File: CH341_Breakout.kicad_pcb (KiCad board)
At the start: 2 copper layers, 4 parts, among them J01 CONN_MODE, J11 CONN_I2C, J12 CONN_UART, J13 CONN_SPI

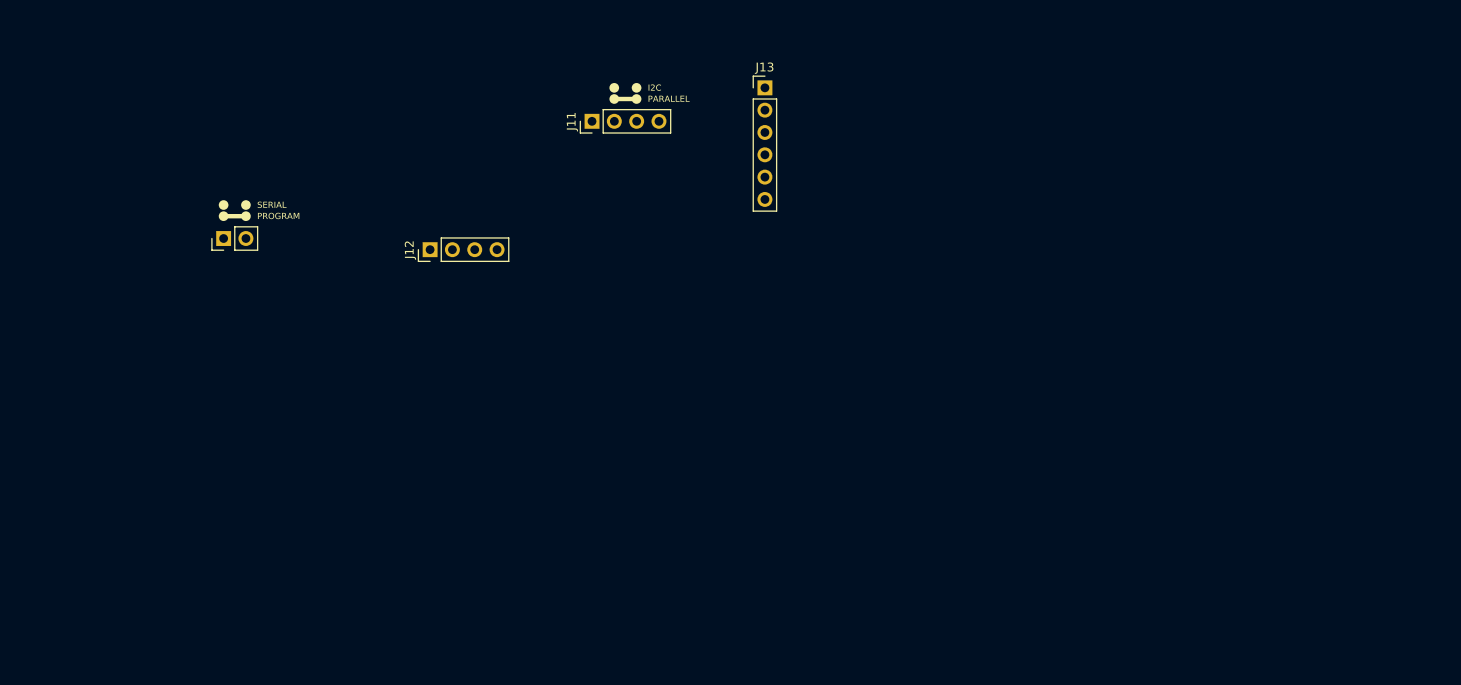
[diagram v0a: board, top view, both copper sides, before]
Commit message: Added USB C and other bits
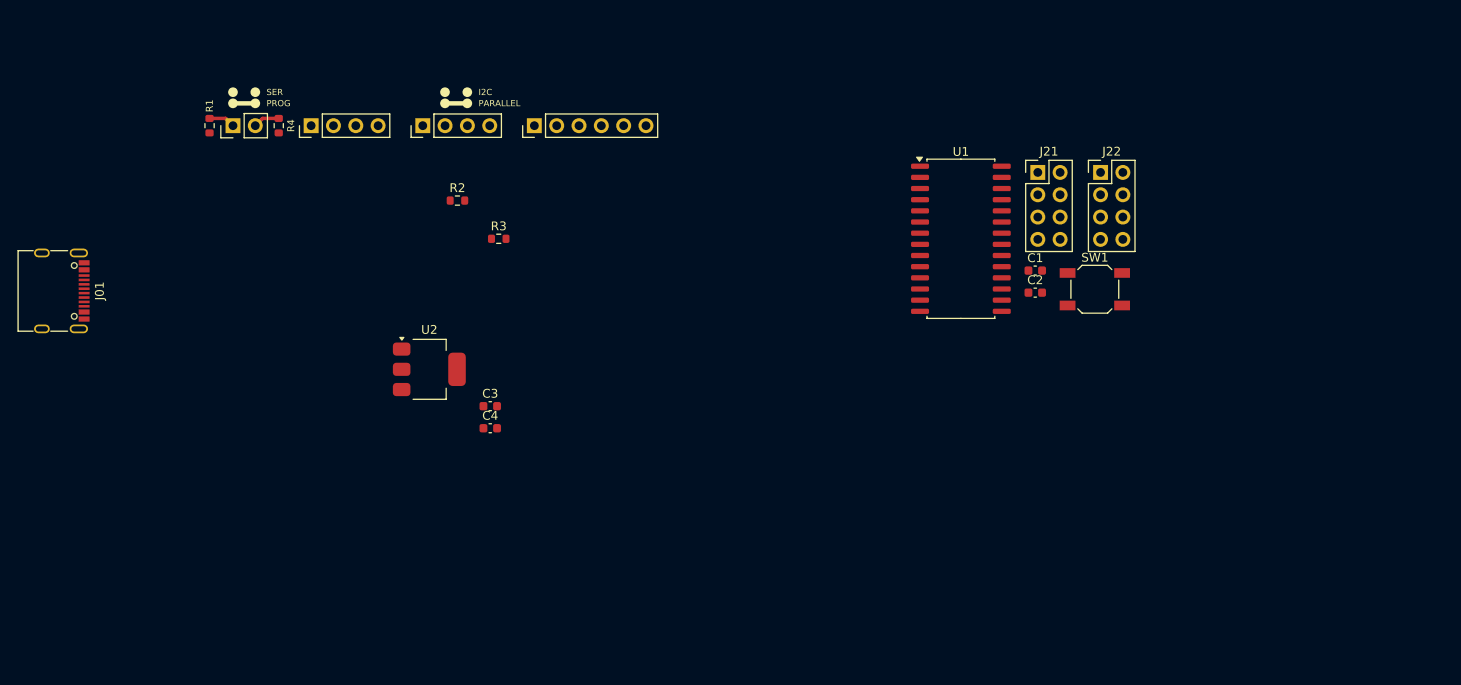
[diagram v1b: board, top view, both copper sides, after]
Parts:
- added C1: 20pF, Capacitor_SMD:C_0603_1608Metric, F.Cu at (131.1, 44.3)
- added C2: 20pF, Capacitor_SMD:C_0603_1608Metric, F.Cu at (131.1, 46.8)
- added C3: 100nF, Capacitor_SMD:C_0603_1608Metric, F.Cu at (69.1, 59.7)
- added C4: 100nF, Capacitor_SMD:C_0603_1608Metric, F.Cu at (69.1, 62.2)
- added J02: CONN_MODE, Connector_PinHeader_2.54mm:PinHeader_1x02_P2.54mm_Vertical, F.Cu at (39.8, 27.8)
- added J21: CONN_SPI_FLASH, Connector_PinHeader_2.54mm:PinHeader_2x04_P2.54mm_Vertical, F.Cu at (131.4, 33.1)
- added J22: CONN_I2C_EEPROM, Connector_PinHeader_2.54mm:PinHeader_2x04_P2.54mm_Vertical, F.Cu at (138.5, 33.1)
- added R1: 2K2, Resistor_SMD:R_0603_1608Metric, F.Cu at (37.1, 27.8)
- added R2: 2K2, Resistor_SMD:R_0603_1608Metric, F.Cu at (65.3, 36.3)
- added R3: 2K2, Resistor_SMD:R_0603_1608Metric, F.Cu at (70.0, 40.7)
- added R4: 2K2, Resistor_SMD:R_0603_1608Metric, F.Cu at (45.0, 27.8)
- added SW1: SW_SPST, Button_Switch_SMD:SW_SPST_SKQG_WithoutStem, F.Cu at (137.9, 46.4)
- added U1: CH341A, Package_SO:SOIC-28W_7.5x17.9mm_P1.27mm, F.Cu at (122.6, 40.7)
- added U2: AMS1117-3.3, Package_TO_SOT_SMD:SOT-223-3_TabPin2, F.Cu at (62.1, 55.5)
- J01: value CONN_MODE -> USB_C; footprint Connector_PinHeader_2.54mm:PinHeader_1x02_P2.54mm_Vertical -> Connector_USB:USB_C_Receptacle_G-Switch_GT-USB-7010ASV
- moved J13 26.6 mm to (74.1, 27.8), turned to 90 degrees
- moved J01 20.5 mm to (19.1, 46.6), turned to -90 degrees
- moved J12 19.6 mm to (48.7, 27.8)
- moved J11 19.3 mm to (61.4, 27.8)
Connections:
- J11 pad 4: /A0 -> GND
- J12 pad 4: /A0 -> GND
- J13 pad 6: /A0 -> GND
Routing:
- net Net-(J02-Pin_2): track 0.00 -> 3.01 mm
- net /ACT#: track 0.00 -> 3.01 mm
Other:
- board text added: "3V3"
- board text added: "CS"
- board text added: "GND"
- board text added: "MISO"
- board text added: "MOSI"
- board text added: "PROG"
- board text added: "RX"
- board text added: "SCL"
- board text added: "SCLK"
- board text added: "SDA"
- board text added: "SER"
- board text added: "TX"
- board text removed: "PROGRAM"
- board text removed: "SERIAL"

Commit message: Started MkI PCB Design
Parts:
- removed C4: 100nF, Capacitor_SMD:C_0603_1608Metric
- removed the J11 at (61.4, 27.8)
- removed the J13 at (74.1, 27.8)
- added D1: ACT, LED_SMD:LED_0603_1608Metric, F.Cu at (174.3, 84.3)
- added D2: PWR, LED_SMD:LED_0603_1608Metric, F.Cu at (174.3, 87.5)
- added Y1: 12MHz, Crystal:Crystal_HC49-U_Vertical, F.Cu at (153.9, 75.5)
- J12: renamed from J22; value CONN_I2C_EEPROM -> CONN_SPI_FLASH
- SW1: value SW_SPST -> RST
- moved J01 148.8 mm to (163.0, 84.7), turned to 0 degrees
- moved R1 147.8 mm to (174.3, 82.7), turned to 180 degrees
- moved J02 144.3 mm to (174.3, 80.1), turned to 180 degrees
- moved R4 137.6 mm to (174.3, 74.9), turned to 0 degrees
- moved J11 132.1 mm to (174.3, 68.7), turned to 180 degrees
- moved R2 119.7 mm to (174.3, 85.9), turned to 180 degrees
- moved C3 98.4 mm to (167.5, 59.8), turned to 180 degrees
- moved U2 95.3 mm to (153.1, 84.0), turned to -90 degrees
- moved R3 83.8 mm to (150.1, 65.4), turned to 90 degrees
- moved U1 49.8 mm to (163.0, 69.8)
- moved J13 40.4 mm to (165.5, 54.6), turned to 90 degrees
- moved C1 37.2 mm to (150.1, 76.3), turned to -90 degrees
- moved C2 29.8 mm to (150.1, 69.8), turned to 90 degrees
- moved J12 25.8 mm to (152.8, 54.6), turned to 90 degrees
- moved SW1 22.7 mm to (153.8, 62.6), turned to -90 degrees
- renumbered J12 to J11, J21 to J13
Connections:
- net /SPI_CLK renamed /SPI_SCLK
- C3 pad 1: Net-(U2-VI) -> VBUS_3V3
- J11 pad 1: /SPI_HOLD -> VBUS_3V3
- J12 pad 2: GND -> VBUS_3V3
- J12 pad 5: /I2C_SDA -> GND
- J12 pad 8: /SPI_HOLD -> /I2C_SDA
- J13 pad 2: /SPI_MISO -> VBUS_3V3
- J13 pad 3: /SPI_HOLD -> /SPI_MISO
- J13 pad 4: GND -> VBUS_3V3
- J13 pad 5: /SPI_MOSI -> VBUS_3V3
- J13 pad 7: /SPI_HOLD -> GND
- J13 pad 8: /SPI_HOLD -> /SPI_MOSI
- R1 pad 1: unconnected-(R1-Pad1) -> Net-(D1-K)
- R2 pad 1: unconnected-(R2-Pad1) -> Net-(D2-K)
- SW1 pad 2: /SPI_HOLD -> VBUS_3V3
- U1 pad 28: /SPI_HOLD -> VBUS_3V3
- U1 pad 9: /SPI_HOLD -> VBUS_3V3
- U2 pad 2: /SPI_HOLD -> VBUS_3V3
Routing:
- net /SPI_CS: track 0.00 -> 25.2 mm
- net /SPI_SCLK: track 0.00 -> 24.9 mm
- net /SPI_MOSI: track 0.00 -> 23.8 mm, vias 0 -> 1
- net /UART_TX: track 0.00 -> 20.8 mm, vias 0 -> 1
- net /I2C_SDA: track 0.00 -> 20.5 mm, vias 0 -> 1
- net /I2C_SCL: track 0.00 -> 19.9 mm, vias 0 -> 1
- net /UART_RX: track 0.00 -> 18.2 mm, vias 0 -> 1
- net Net-(U2-VI): track 0.00 -> 17.9 mm, vias 0 -> 3
- net /SPI_MISO: track 0.00 -> 17.0 mm
- net Net-(U1-XI): track 0.00 -> 12.0 mm
- net /USB_DP: track 0.00 -> 12.0 mm
- net /USB_DN: track 0.00 -> 11.4 mm
- net Net-(U1-XO): track 0.00 -> 9.18 mm
- net GND: track 0.00 -> 8.88 mm, vias 0 -> 6
- net VBUS_3V3: track 0.00 -> 8.34 mm, vias 0 -> 2
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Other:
- board outline added: 28 x 42 mm
- board text added: "A0"
- board text added: "A1"
- board text added: "A2"
- board text added: "ACT"
- board text added: "HOLD"
- board text added: "I2C EEPROM"
- board text added: "PWR"
- board text added: "SPI FLASH"
- board text added: "V+"
- board text added: "WP"
- board text removed: "I2C"
- board text removed: "PARALLEL"

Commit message: Finished MkI Board
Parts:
- J12: value CONN_SPI_FLASH -> CONN_I2C_EEPROM
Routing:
- net VBUS_3V3: track 8.34 -> 126.1 mm, vias 2 -> 7
- net /ACT#: track 2.94 -> 32.0 mm
- net /RESET: track 0.00 -> 11.8 mm
- net GND: track 8.88 -> 11.5 mm, vias 6 -> 31
- net /SPI_MOSI: track 23.8 -> 21.8 mm, vias 1 -> 2
- added copper zone on B.Cu, net GND
- added copper zone on F.Cu, net GND
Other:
- board text added: "USB-C CH341A Breakout ADBeta MkI 28 Apr '25"

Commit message: Finalised, built and tested
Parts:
- moved C3 135.4 mm to (35.7, 28.9)
- moved D1 135.4 mm to (42.5, 53.4)
- moved D2 135.4 mm to (42.5, 56.6)
- moved J01 135.4 mm to (31.2, 53.8)
- moved J11 135.4 mm to (42.5, 37.8)
- moved J12 135.4 mm to (21.0, 23.7)
- moved R1 135.4 mm to (42.5, 51.8)
- moved R2 135.4 mm to (42.5, 55.0)
- moved R3 135.4 mm to (18.3, 34.5)
- moved R4 135.4 mm to (42.5, 44.0)
- moved U1 135.4 mm to (31.2, 38.9)
- moved U2 135.4 mm to (21.3, 53.1)
- moved Y1 135.4 mm to (22.1, 44.6)
- moved C1 135.4 mm to (18.3, 45.4)
- moved C2 135.4 mm to (18.3, 38.9)
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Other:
- outline, holes or cut-outs redrawn
- board text added: "USB-C CH341A Breakout ADBeta MkI 09 May '25"
- board text removed: "USB-C CH341A Breakout ADBeta MkI 28 Apr '25"
